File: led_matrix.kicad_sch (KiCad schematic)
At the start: 107 parts, among them J1 I2C, J2 Extra, J3 Address, J4 +5V, J5 GND, J6 Power Input, Q1 2N3904, Q2 2N3904, Q3 2N3904, Q4 2N3904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

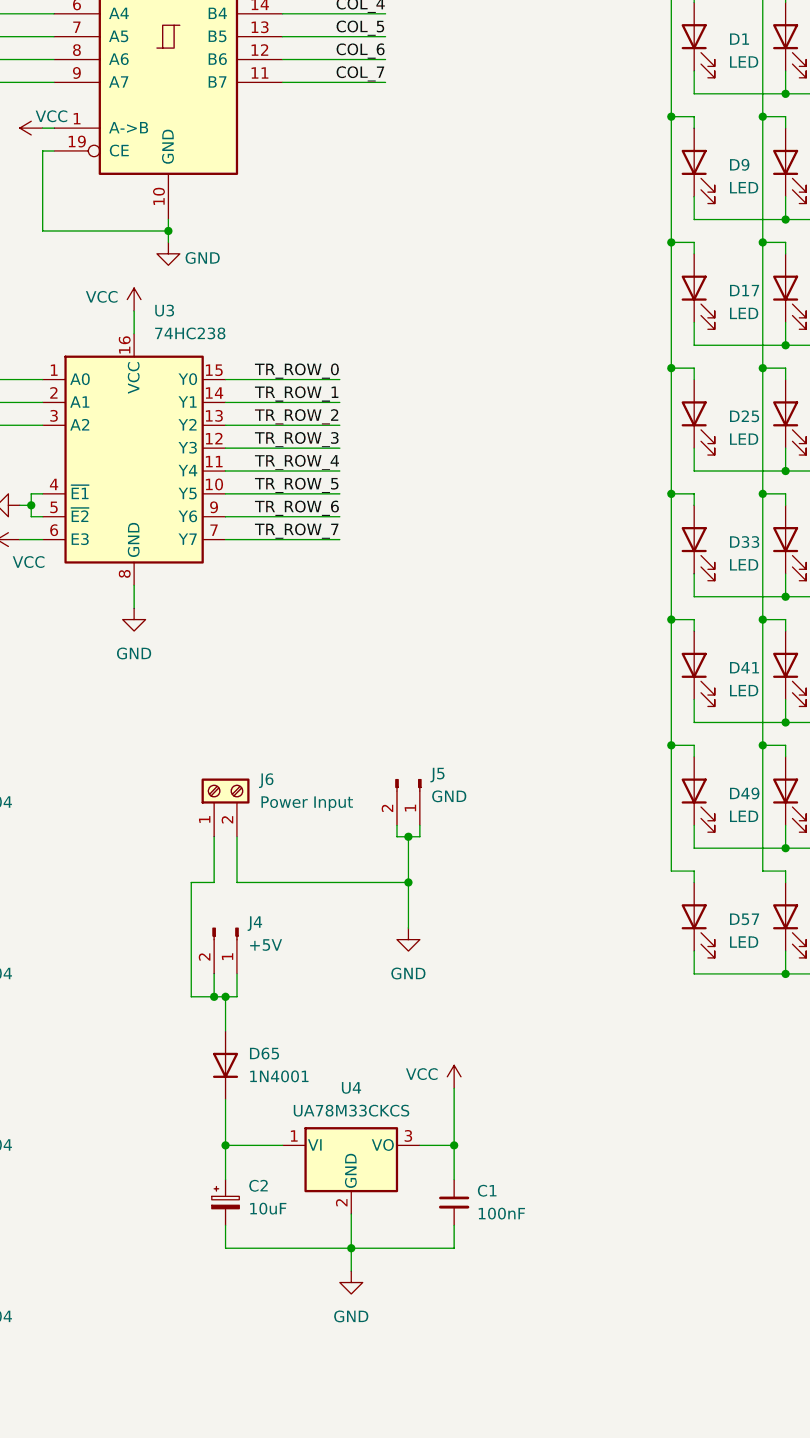
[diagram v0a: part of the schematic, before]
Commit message: Add holes and caps
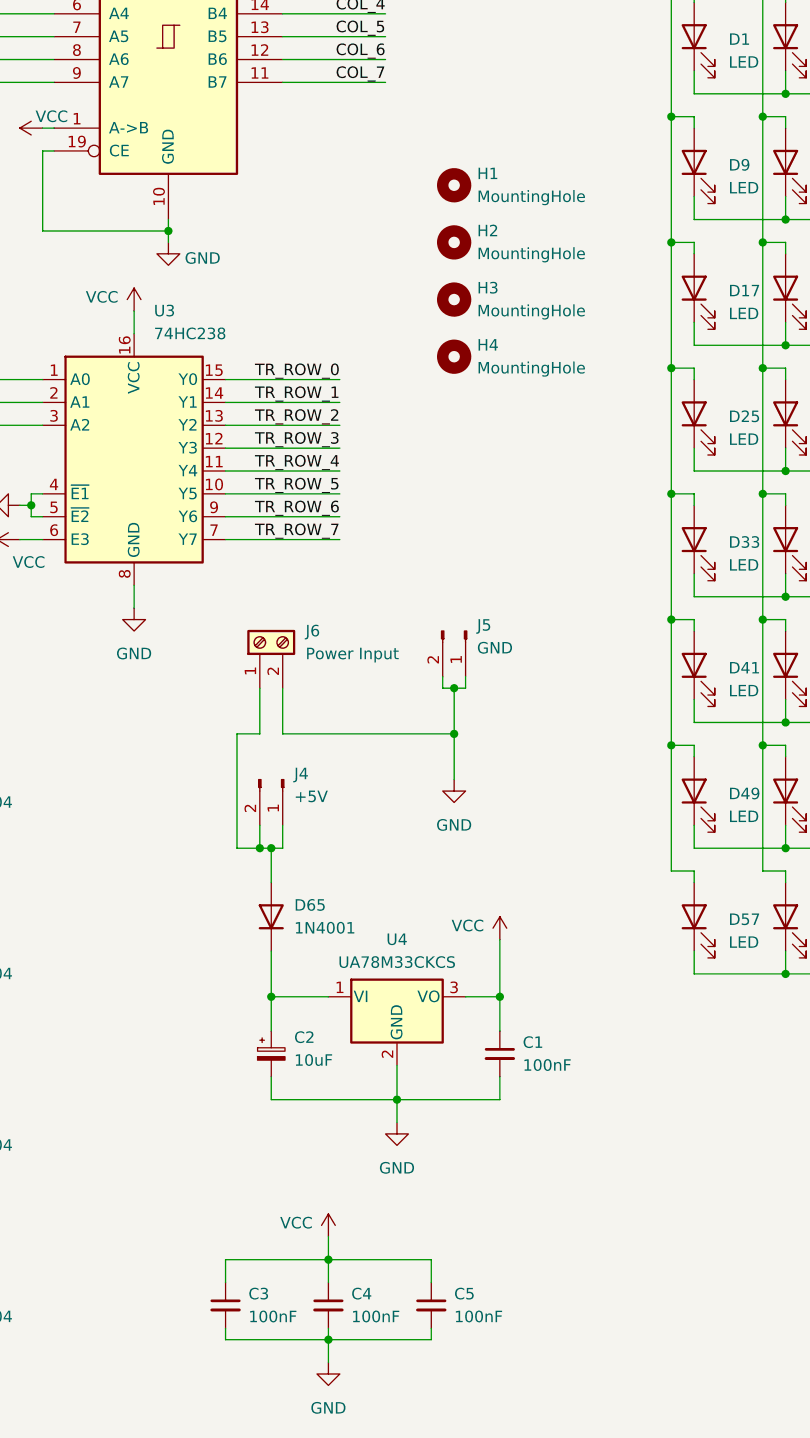
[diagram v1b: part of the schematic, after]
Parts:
- added C3, C4, C5: 100nF, Capacitor_THT:C_Disc_D7.0mm_W2.5mm_P5.00mm, symbol Device:C_Small
- added H1, H2, H3, H4: MountingHole, MountingHole:MountingHole_3.2mm_M3_DIN965, symbol Mechanical:MountingHole
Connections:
- net GND: now also C3.2, C4.2, C5.2
- net VCC: now also C3.1, C4.1, C5.1
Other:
- moved on the sheet: C1, C2, D65, J4, J5, J6, U4

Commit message: Update project
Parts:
- added J7: Columns, Connector_PinHeader_2.54mm:PinHeader_1x08_P2.54mm_Vertical, symbol Connector:Conn_01x08_Pin
- added J8: Row Addr., Connector_PinHeader_2.54mm:PinHeader_1x03_P2.54mm_Vertical, symbol Connector:Conn_01x03_Pin
- C2: footprint Capacitor_THT:CP_Radial_D8.0mm_P3.80mm -> Capacitor_THT:CP_Radial_D6.3mm_P2.50mm
- Q1, Q2, Q3, Q4, Q5, Q6, Q7, Q8: footprint Package_TO_SOT_THT:TO-92_Inline -> Package_TO_SOT_THT:TO-92_HandSolder
- U2: value 74AC45 -> 74AC245
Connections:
- net COL_0: now also U1.1 (GPB0), U2.2 (A0), J7.1 (Pin_1); no longer R9.2, U2.18 (B0)
- net COL_1: now also U1.2 (GPB1), U2.3 (A1), J7.2 (Pin_2); no longer R10.2, U2.17 (B1)
- net COL_2: now also U1.3 (GPB2), U2.4 (A2), J7.3 (Pin_3); no longer R11.2, U2.16 (B2)
- net COL_3: now also U1.4 (GPB3), U2.5 (A3), J7.4 (Pin_4); no longer R12.2, U2.15 (B3)
- net COL_4: now also U1.5 (GPB4), U2.6 (A4), J7.5 (Pin_5); no longer R13.2, U2.14 (B4)
- net COL_5: now also U1.6 (GPB5), U2.7 (A5), J7.6 (Pin_6); no longer R14.2, U2.13 (B5)
- net COL_6: now also U1.7 (GPB6), U2.8 (A6), J7.7 (Pin_7); no longer R15.2, U2.12 (B6)
- net COL_7: now also U1.8 (GPB7), U2.9 (A7), J7.8 (Pin_8); no longer R16.2, U2.11 (B7)
- net RECT_5V: now reaches C2.1, D65.1 (K), U4.1 (VI)
- net +5V: now reaches D65.2 (A), J4.1 (Pin_1), J4.2 (Pin_2), J6.1 (Pin_1)
- net at J2.1 (Pin_1): now also U1.20 (INTA); no longer U1.19 (INTB)
- net at J2.2 (Pin_2): now also U1.19 (INTB); no longer U1.20 (INTA)
- net at U1.21 (GPA0): no longer U3.1 (A0)
- net at U1.22 (GPA1): no longer U3.2 (A1)
- net at U1.23 (GPA2): no longer U3.3 (A2)
- net R_ADDR_2: now reaches U1.26 (GPA5)
- net R_ADDR_2: now also U3.3 (A2), J8.3 (Pin_3)
- net R_ADDR_1: now reaches U1.27 (GPA6)
- net R_ADDR_1: now also U3.2 (A1), J8.2 (Pin_2)
- net R_ADDR_0: now reaches U1.28 (GPA7)
- net R_ADDR_0: now also U3.1 (A0), J8.1 (Pin_1)
- new net B_COL_0: R9.2, U2.18 (B0)
- new net B_COL_1: R10.2, U2.17 (B1)
- new net B_COL_2: R11.2, U2.16 (B2)
- new net B_COL_3: R12.2, U2.15 (B3)
- new net B_COL_4: R13.2, U2.14 (B4)
- new net B_COL_5: R14.2, U2.13 (B5)
- new net B_COL_6: R15.2, U2.12 (B6)
- new net B_COL_7: R16.2, U2.11 (B7)

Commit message: Update PCB
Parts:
- R17, R18: value 1K -> DNF
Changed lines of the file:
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@@
 			)
 		)
-		(property "Value" "1K"
+		(property "Value" "DNF"
 			(at 44.704 36.068 90)
 			(effects
@@
 			)
 		)
-		(property "Value" "1K"
+		(property "Value" "DNF"
 			(at 48.514 36.068 90)
 			(effects

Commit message: Update silkscreen a bit
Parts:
- U1: value MCP23017_SP -> MCP23017
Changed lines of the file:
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@@
 			)
 		)
-		(property "Value" "MCP23017_SP"
+		(property "Value" "MCP23017"
 			(at 73.3141 39.37 0)
 			(effects

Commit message: Update board organization, silkscreen and power regulator placement
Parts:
- U4: footprint Package_TO_SOT_THT:TO-220-3_Vertical -> Package_TO_SOT_THT:TO-220-3_Horizontal_TabDown
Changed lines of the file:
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@@
 			)
 		)
-		(property "Footprint" "Package_TO_SOT_THT:TO-220-3_Vertical"
+		(property "Footprint" "Package_TO_SOT_THT:TO-220-3_Horizontal_TabDown"
 			(at 143.51 144.145 0)
 			(effects

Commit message: Enlarge mounting holes
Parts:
- H1, H2, H3, H4: footprint MountingHole:MountingHole_3.2mm_M3_DIN965 -> MountingHole:MountingHole_3.5mm
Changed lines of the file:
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@@
 			)
 		)
-		(property "Footprint" "MountingHole:MountingHole_3.2mm_M3_DIN965"
+		(property "Footprint" "MountingHole:MountingHole_3.5mm"
 			(at 149.86 59.69 0)
 			(effects
@@
 			)
 		)
-		(property "Footprint" "MountingHole:MountingHole_3.2mm_M3_DIN965"
+		(property "Footprint" "MountingHole:MountingHole_3.5mm"
 			(at 149.86 66.04 0)
 			(effects
@@
 			)
 		)
-		(property "Footprint" "MountingHole:MountingHole_3.2mm_M3_DIN965"
+		(property "Footprint" "MountingHole:MountingHole_3.5mm"
 			(at 149.86 72.39 0)
 			(effects
@@
 			)
 		)
-		(property "Footprint" "MountingHole:MountingHole_3.2mm_M3_DIN965"
+		(property "Footprint" "MountingHole:MountingHole_3.5mm"
 			(at 149.86 78.74 0)
 			(effects

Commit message: Added an header to pick VCC after the regulator
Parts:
- added J9: VCC, Connector_PinHeader_2.54mm:PinHeader_1x02_P2.54mm_Vertical, symbol Connector:Conn_01x02_Pin
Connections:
- net VCC: now also J9.1 (Pin_1), J9.2 (Pin_2)
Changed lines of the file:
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@@
 	)
 	(junction
+		(at 161.29 149.86)
+		(diameter 0)
+		(color 0 0 0 0)
+	)
+	(junction
 		(at 102.87 95.25)
 		(diameter 0)
@@
 	(wire
 		(pts
+			(xy 163.83 149.86) (xy 163.83 146.05)
+		)
+		(stroke
+			(width 0)
+			(type default)
+		)
+	)
+	(wire
+		(pts
 			(xy 214.63 121.92) (xy 217.17 121.92)
 		)
@@
 	(wire
 		(pts
+			(xy 161.29 149.86) (xy 163.83 149.86)
+		)
+		(stroke
+			(width 0)
+			(type default)
+		)
+	)
+	(wire
+		(pts
 			(xy 207.01 34.29) (xy 207.01 38.1)
 		)
@@
 	(wire
 		(pts
+			(xy 154.94 149.86) (xy 161.29 149.86)
+		)
+		(stroke
+			(width 0)
+			(type default)
+		)
+	)
+	(wire
+		(pts
 			(xy 207.01 88.9) (xy 207.01 91.44)
 		)
@@
 	(wire
 		(pts
+			(xy 161.29 146.05) (xy 161.29 149.86)
+		)
+		(stroke
+			(width 0)
+			(type default)
+		)
+	)
+	(wire
+		(pts
 			(xy 214.63 107.95) (xy 217.17 107.95)
 		)
@@
 					(unit 1)
 				)
+			)
+		)
+	)
+	(symbol
+		(lib_id "Connector:Conn_01x02_Pin")
+		(at 163.83 140.97 270)
+		(unit 1)
+		(exclude_from_sim no)
+		(in_bom yes)
+		(on_board yes)
+		(dnp no)
+		(fields_autoplaced yes)
+		(property "Reference" "J9"
+			(at 165.1 140.3349 90)
+			(effects
+				(font
+					(size 1.27 1.27)
+				)
+				(justify left)
+			)
+		)
+		(property "Value" "VCC"
+			(at 165.1 142.8749 90)
+			(effects
+				(font
+					(size 1.27 1.27)
+				)
+				(justify left)
+			)
+		)
+		(property "Footprint" "Connector_PinHeader_2.54mm:PinHeader_1x02_P2.54mm_Vertical"
+			(at 163.83 140.97 0)
+			(effects
+				(font
+					(size 1.27 1.27)
+				)
+				(hide yes)
+			)
+		)
+		(property "Datasheet" "~"
+			(at 163.83 140.97 0)
+			(effects
+				(font
+					(size 1.27 1.27)
+				)
+				(hide yes)
+			)
+		)
+		(property "Description" "Generic connector, single row, 01x02, script generated"
+			(at 163.83 140.97 0)
+			(effects
+				(font
+					(size 1.27 1.27)
+				)
+				(hide yes)
+			)
+		)
+		(pin "1"
+		)
+		(pin "2"
+		)
+		(instances
+			(project "led_matrix"
+				(path "/e55853e7-be74-492d-8392-4c67a141003e"
+					(reference "J9")
+					(unit 1)
+				)

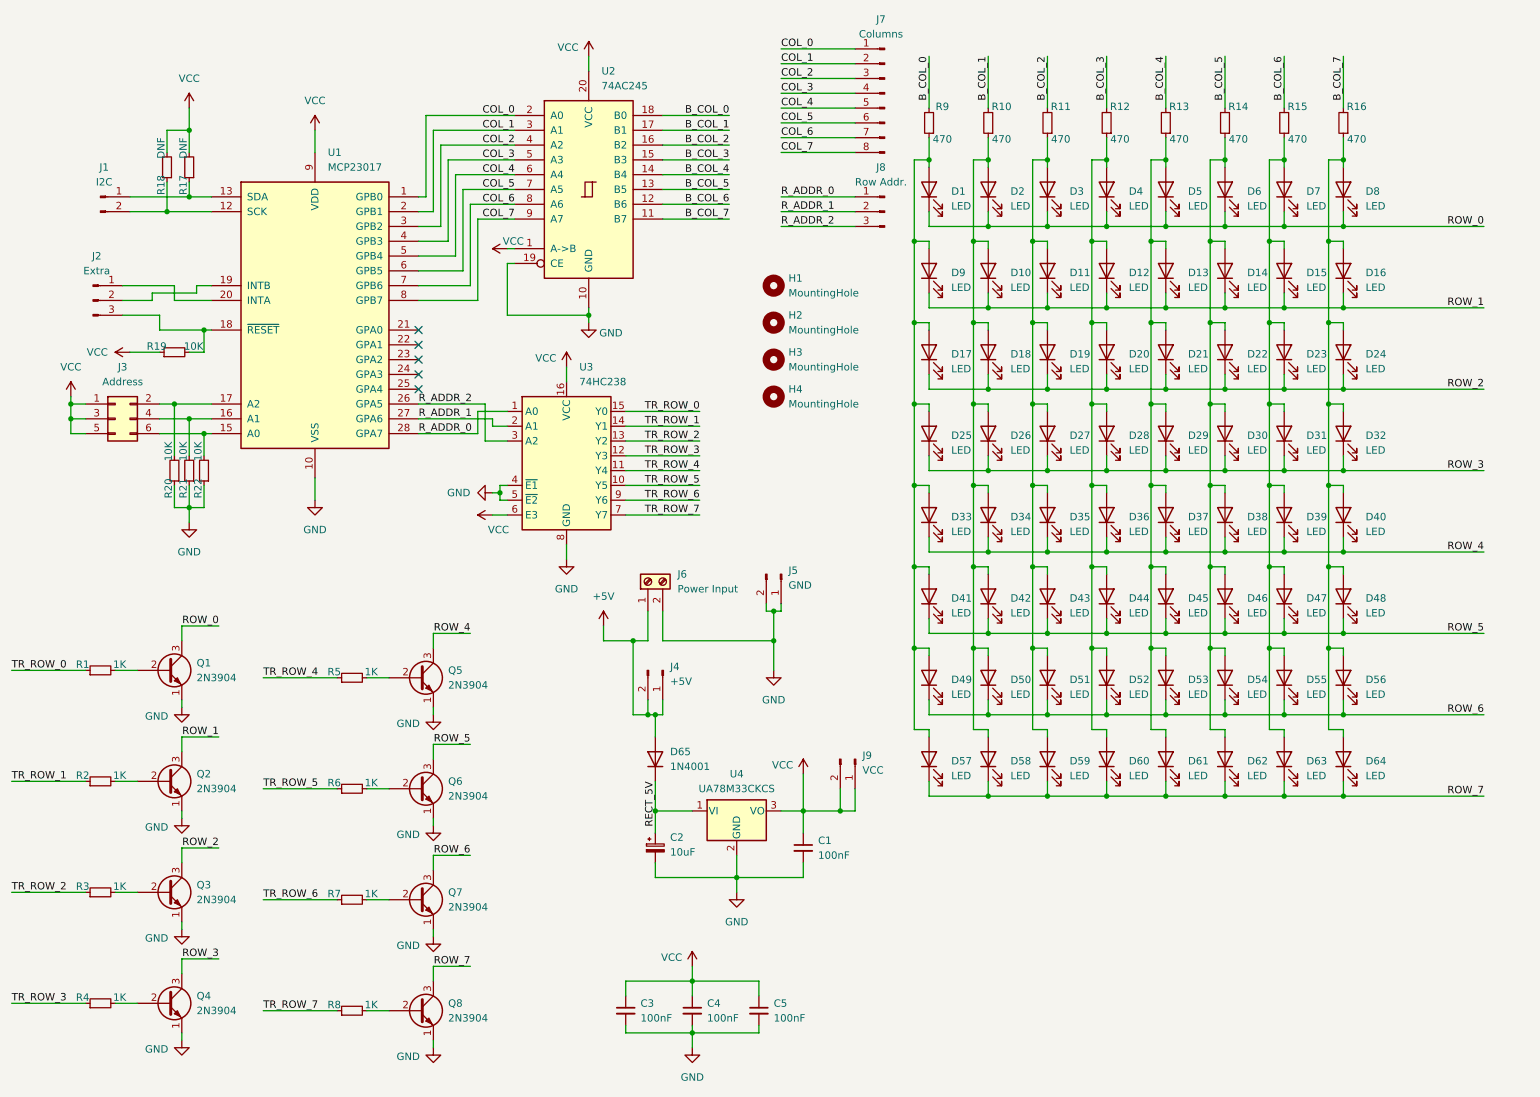
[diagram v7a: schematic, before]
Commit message: Add pulldown resistors to schematic for input pins
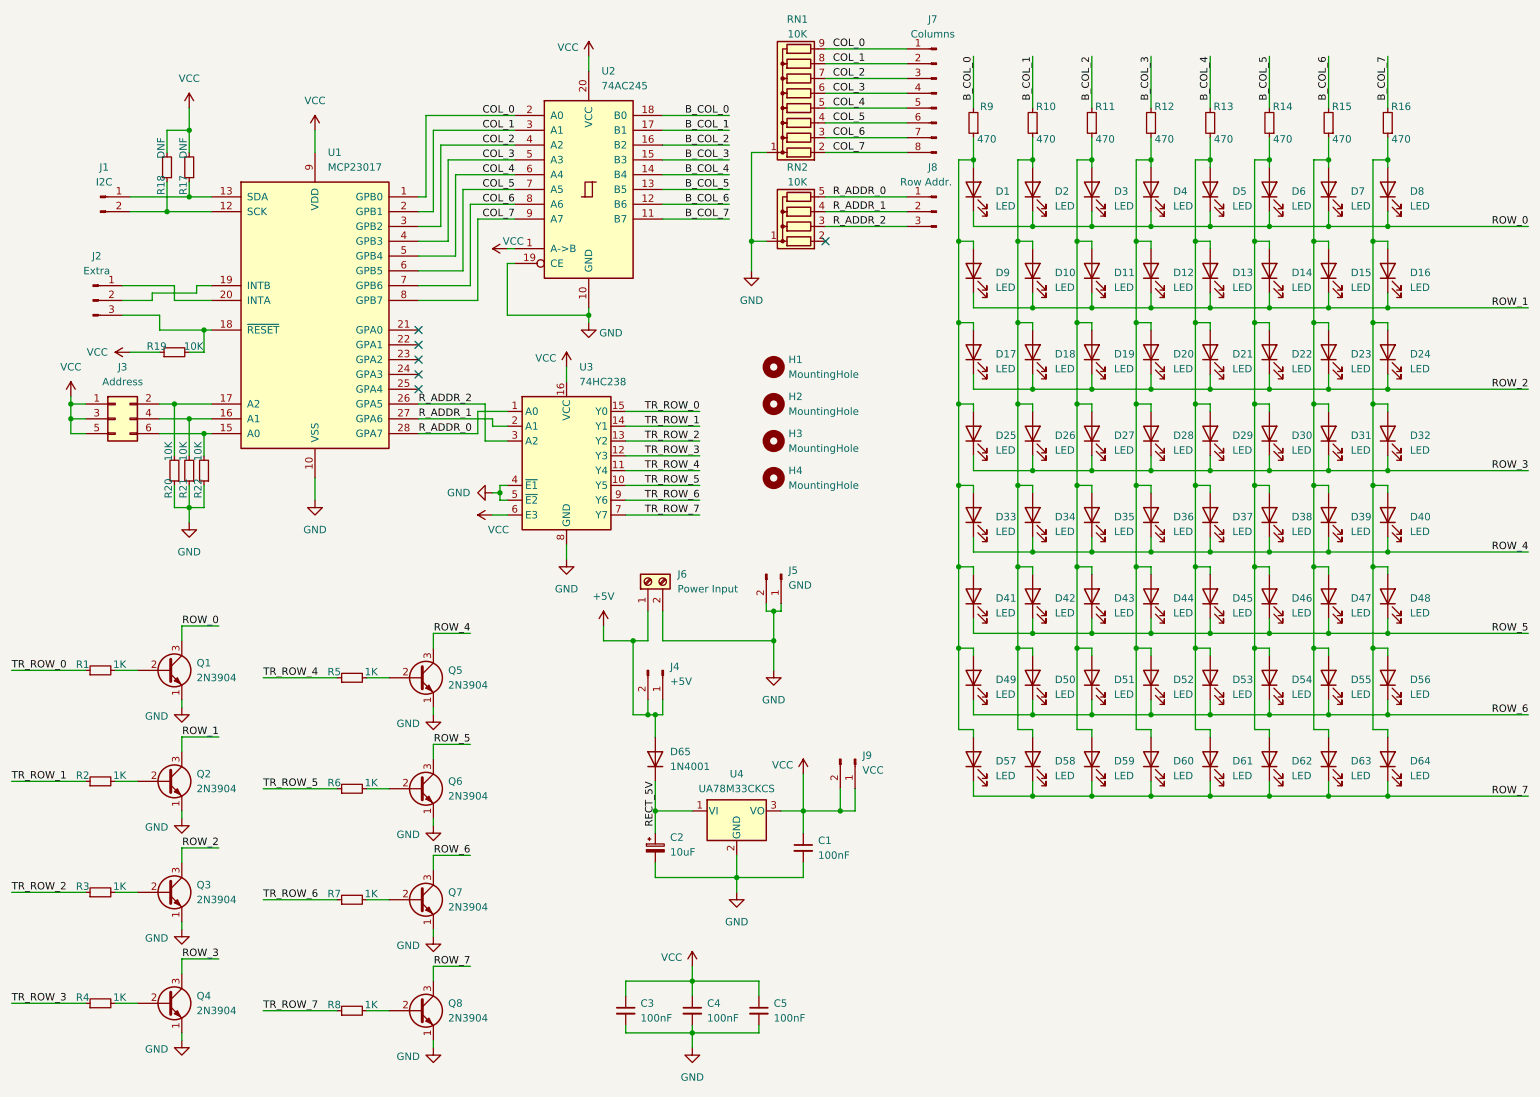
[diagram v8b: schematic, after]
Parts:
- added RN1: 10K, Resistor_THT:R_Array_SIP9, symbol Device:R_Network08
- added RN2: 10K, Resistor_THT:R_Array_SIP5, symbol Device:R_Network04
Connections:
- net COL_0: now also RN1.9 (R8)
- net COL_1: now also RN1.8 (R7)
- net COL_2: now also RN1.7 (R6)
- net COL_3: now also RN1.6 (R5)
- net COL_4: now also RN1.5 (R4)
- net COL_5: now also RN1.4 (R3)
- net COL_6: now also RN1.3 (R2)
- net COL_7: now also RN1.2 (R1)
- net GND: now also RN1.1 (common), RN2.1 (common)
- net R_ADDR_0: now also RN2.5 (R4)
- net R_ADDR_1: now also RN2.4 (R3)
- net R_ADDR_2: now also RN2.3 (R2)
- no-connect marks 5 -> 6
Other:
- moved on the sheet: D1, D10, D11, D12, D13, D14, D15, D16, D17, D18, D19, D2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
